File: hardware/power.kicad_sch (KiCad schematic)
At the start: 28 parts

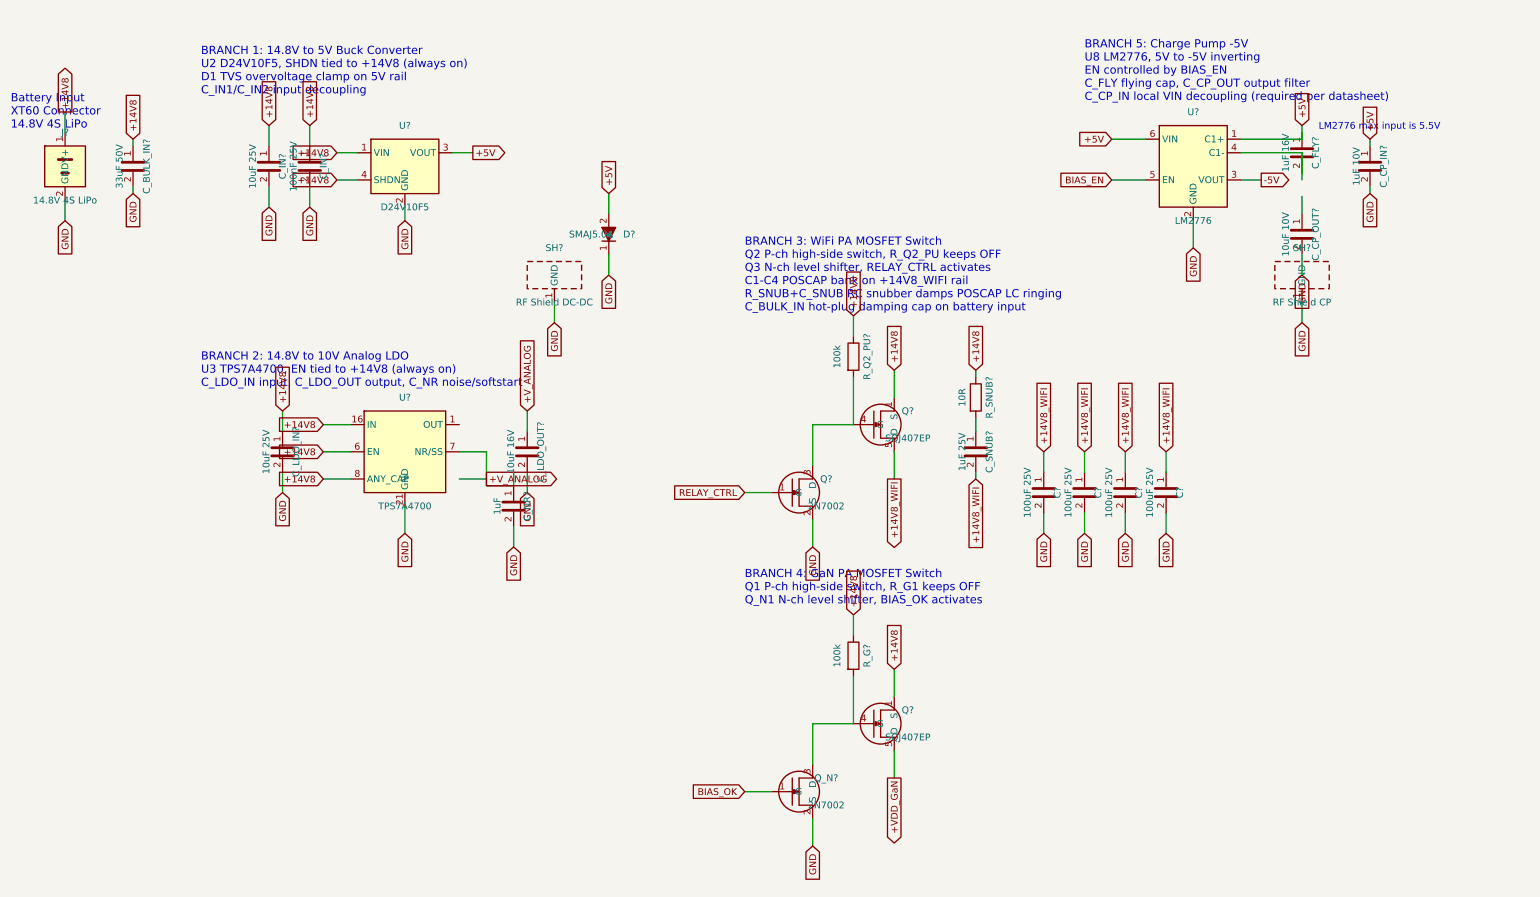
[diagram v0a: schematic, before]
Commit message: jamrf-v2: Add U3V70F15 WiFi PA regulator, FR408HR stackup, full firmware, custom footprints
- Add U3V70F15 buck-boost converter to limit WiFi PA supply to 15V (fixes ZVE-3W-83+ overvoltage)
- Update PCB stackup to Isola FR408HR (Er=3.65, tan d=0.0095) with corrected 0.40mm 50-ohm traces
- Add full operational firmware (main.py): chaos modulation engine, ST7789 display, mode control
- Add 6 custom footprints: M5StickC, Pololu D24V10F5/U3V70F15, Mini-Circuits, Wurth shield, isolator
- Add fp-lib-table and sym-lib-table for custom libraries
- Update README with logo, badges, TIIUAE disclaimer, corrected specs
- Update LICENSE with proper attribution

Co-Authored-By: Claude Opus 4.6 <noreply@anthropic.com>
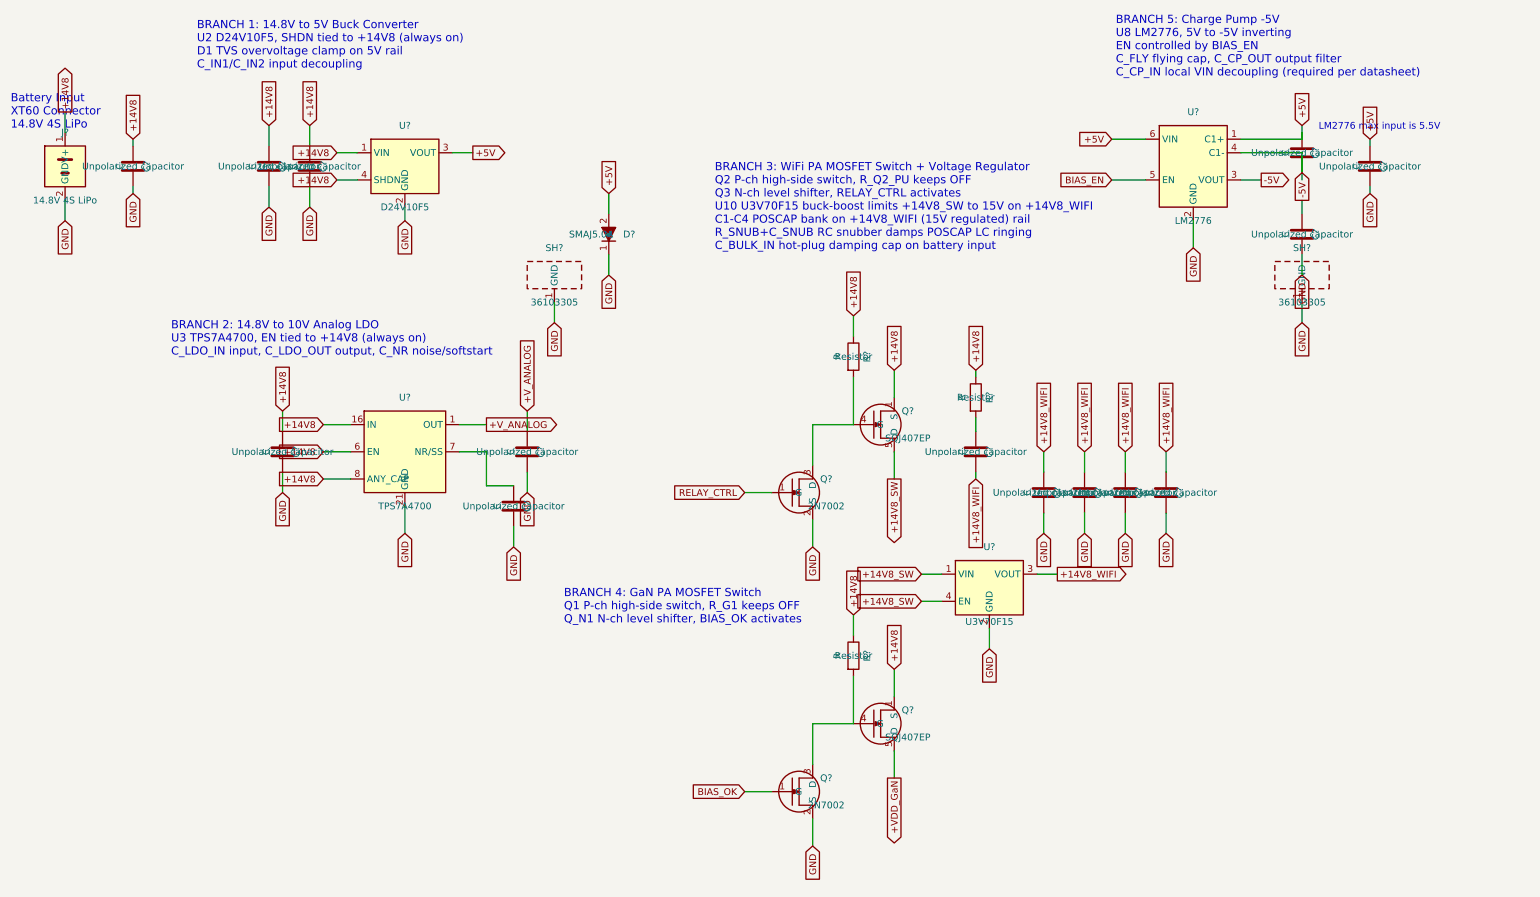
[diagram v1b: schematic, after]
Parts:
- added U?: U3V70F15, jamrf-v2:Pololu_U3V70F15, symbol jamrf-v2:U3V70F15
- C?: renamed from C_IN?; value 10uF 25V -> C
- C?: renamed from C_IN?; value 100nF 25V -> C
- C?: renamed from C_LDO_IN?; value 10uF 25V -> C
- C?: renamed from C_LDO_OUT?; value 10uF 16V -> C
- C?: renamed from C_NR?; value 1uF -> C
- C?: renamed from C_FLY?; value 1uF 16V -> C
- C?: renamed from C_CP_OUT?; value 10uF 10V -> C
- C? (x4): value 100uF 25V -> C
- C?: renamed from C_CP_IN?; value 1uF 10V -> C
- C?: renamed from C_SNUB?; value 1uF 25V -> C
- C?: renamed from C_BULK_IN?; value 33uF 50V -> C
- J?: footprint Connector_XT60:XT60_Horizontal -> Connector_AMASS:AMASS_XT60PW-M_1x02_P7.20mm_Horizontal
- R?: renamed from R_G?; value 100k -> R
- R?: renamed from R_Q2_PU?; value 100k -> R
- R?: renamed from R_SNUB?; value 10R -> R
- SH?: value RF Shield DC-DC -> 36103305
- SH?: value RF Shield CP -> 36103305
- U?: footprint Package_DFN_QFN:QFN-20-1EP_4x4mm_P0.5mm_EP2.45x2.45mm -> Package_DFN_QFN:Texas_RGP0020H_VQFN-20-1EP_4x4mm_P0.5mm_EP2.4x2.4mm
- gave numbers to parts that had none: 1
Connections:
- net +14V8_WIFI: now also U?.3 (VOUT); no longer Q?.5 (D)
- net +V_ANALOG: now also U?.1 (OUT); no longer C?.1, U?.7 (NR/SS)
- net -5V: now also C?.1
- net GND: now also U?.2 (GND)
- new net: C?.1, U?.7 (NR/SS)
- new net +14V8_SW: Q?.5 (D), U?.1 (VIN), U?.4 (EN)
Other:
- note added: "BRANCH 3: WiFi PA MOSFET Switch + Voltage Regulator Q2 P-ch high-side switch, R_Q2_PU keeps OFF Q3 N-ch level shifter, RELAY_CTRL activates U10 U3V70F15 buck-boost limits +14V8_SW to 15V on +14V8_WIFI C1-C4 POSCAP bank on +14V8_WIFI (15V regulated) rail R_SNUB+C_SNUB RC snubber damps POSCAP LC ringing C_BULK_IN hot-plug damping cap on battery input"
- note removed: "BRANCH 3: WiFi PA MOSFET Switch Q2 P-ch high-side switch, R_Q2_PU keeps OFF Q3 N-ch level shifter, RELAY_CTRL activates C1-C4 POSCAP bank on +14V8_WIFI rail R_SNUB+C_SNUB RC snubber damps POSCAP LC ringing C_BULK_IN hot-plug damping cap on battery input"

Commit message: Annotate all component references and update CLAUDE.md
- All component references annotated (U1-U10, R1-R17, C1-C19, Q1-Q4, etc.)
- Fix CLAUDE.md: correct jamrf-v4 description (dual-band, not WiFi-only)
- Update CLAUDE.md: file paths match main branch structure, add firmware docs
- Remove resolved known issues (annotation, footprint library)

Co-Authored-By: Claude Opus 4.6 <noreply@anthropic.com>
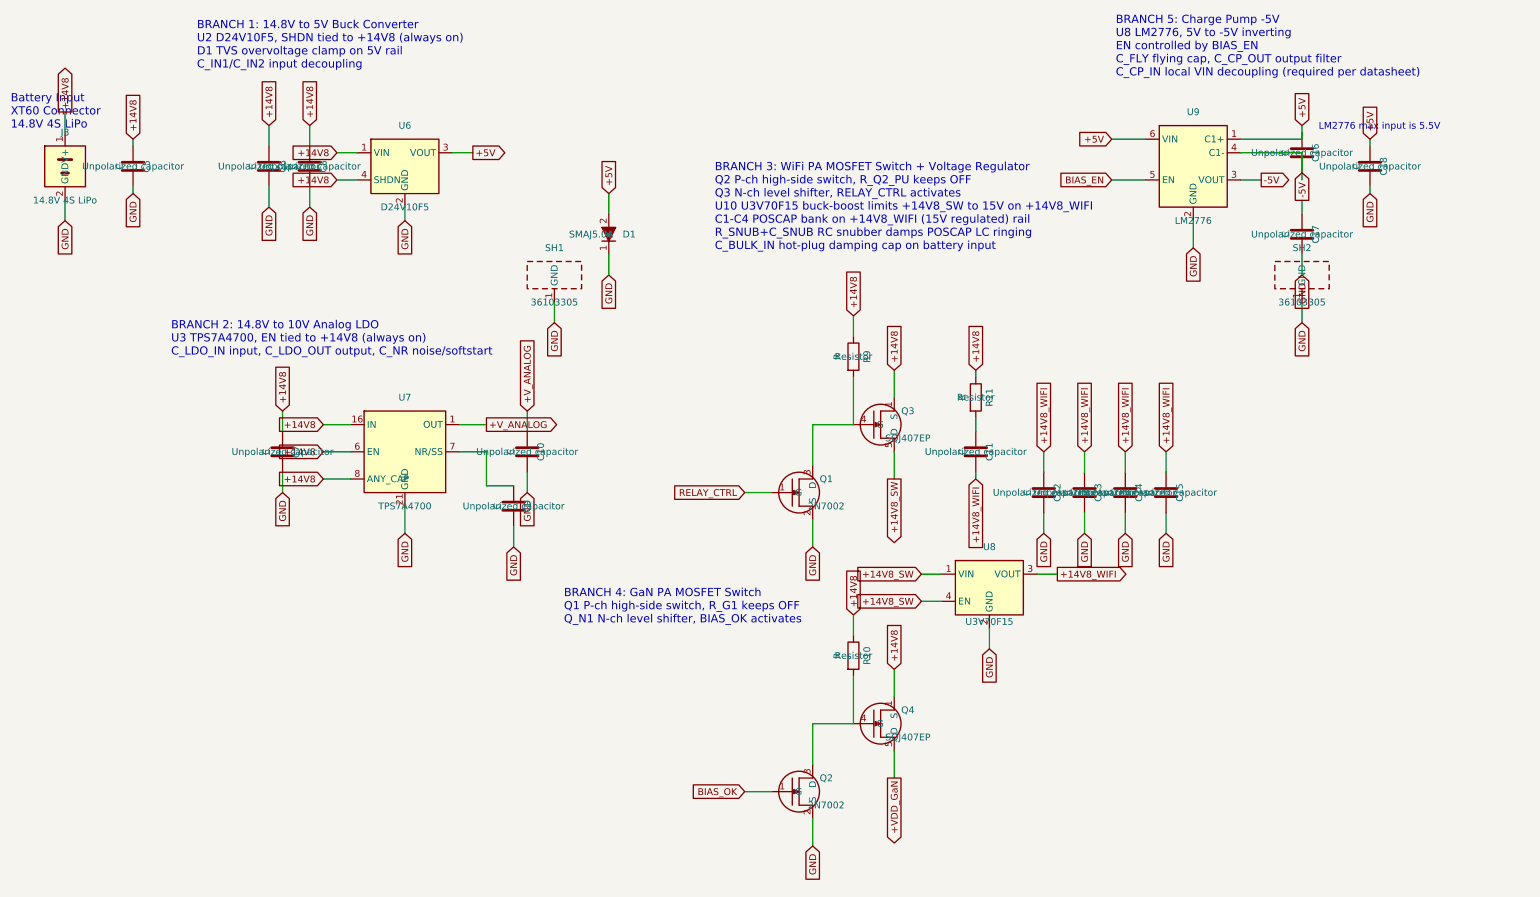
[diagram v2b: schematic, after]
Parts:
- gave numbers to parts that had none: 29
